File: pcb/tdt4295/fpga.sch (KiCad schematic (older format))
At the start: 1 part

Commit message: start implementing FPGA spi flash
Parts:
- removed U?: XC7A100T-FTG256, symbol FPGA_Xilinx_Artix7:XC7A100T-FTG256
- added J1: FPGA__debug, symbol Connector_Generic:Conn_02x07_Odd_Even
- added U?: XC7A100T-FTG256, symbol FPGA_Xilinx_Artix7:XC7A100T-FTG256
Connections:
- net labels added: GND
- wire segments 0 -> 7
- no-connect marks 23 -> 1
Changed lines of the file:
@@
 $Descr A4 11693 8268
 encoding utf-8
-Sheet 5 5
+Sheet 1 1
 Title ""
 Date ""
@@
 Comment4 ""
 $EndDescr
+NoConn ~ -700 1050
 $Comp
 L FPGA_Xilinx_Artix7:XC7A100T-FTG256 U?
-U 1 1 6142E77A
-P 4650 3800
-F 0 "U?" H 4650 825 50  0000 C CNN
-F 1 "XC7A100T-FTG256" H 4650 734 50  0000 C CNN
-F 2 "" H 4650 3800 50  0001 C CNN
-F 3 "" H 4650 3800 50  0000 C CNN
-	1    4650 3800
+U 3 1 6143113A
+P 4700 3350
+F 0 "U?" H 3420 3403 50  0000 R CNN
+F 1 "XC7A100T-FTG256" H 3420 3312 50  0000 R CNN
+F 2 "" H 4700 3350 50  0001 C CNN
+F 3 "" H 4700 3350 50  0000 C CNN
+	3    4700 3350
+	-1   0    0    -1
+$EndComp
+$Comp
+L Connector_Generic:Conn_02x07_Odd_Even J1
+U 1 1 6145021F
+P 800 2850
+F 0 "J1" H 850 3367 50  0000 C CNN
+F 1 "FPGA__debug" H 850 3276 50  0000 C CNN
+F 2 "" H 800 2850 50  0001 C CNN
+F 3 "~" H 800 2850 50  0001 C CNN
+	1    800  2850
 	1    0    0    -1
 $EndComp
-NoConn ~ 2650 1700
-NoConn ~ 2650 2300
-NoConn ~ 2650 2400
-NoConn ~ 2650 2500
-NoConn ~ 2650 2600
-NoConn ~ 2650 2700
-NoConn ~ 2650 2900
-NoConn ~ 2650 3000
-NoConn ~ 2650 3100
-NoConn ~ 2650 3200
-NoConn ~ 2650 3300
-NoConn ~ 2650 3400
-NoConn ~ 2650 3500
-NoConn ~ 2650 3600
-NoConn ~ 2650 3700
-NoConn ~ 2650 3800
-NoConn ~ 2650 3900
-NoConn ~ 2650 4000
-NoConn ~ 2650 4100
-NoConn ~ 2650 4300
-NoConn ~ 2650 4400
-NoConn ~ 2650 4500
-NoConn ~ -700 1050
+Wire Wire Line
+	600  2550 600  2650
+Connection ~ 600  2650
+Wire Wire Line
+	600  2650 600  2750
+Connection ~ 600  2750
+Wire Wire Line
+	600  2750 600  2850
+Connection ~ 600  2850
+Wire Wire Line
+	600  2850 600  2950
+Connection ~ 600  2950
+Wire Wire Line
+	600  2950 600  3050
+Connection ~ 600  3050
+Wire Wire Line
+	600  3050 600  3150
+Connection ~ 600  3150
+Wire Wire Line
+	600  3150 600  3350
+$Comp
+L power:GND #PWR?
+U 1 1 61452A07
+P 600 3350
+F 0 "#PWR?" H 600 3100 50  0001 C CNN
+F 1 "GND" H 605 3177 50  0000 C CNN
+F 2 "" H 600 3350 50  0001 C CNN
+F 3 "" H 600 3350 50  0001 C CNN
+	1    600  3350
+	1    0    0    -1
+$EndComp
 $EndSCHEMATC

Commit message: fpga and vga
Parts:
- removed U?: XC7A100T-FTG256, symbol FPGA_Xilinx_Artix7:XC7A100T-FTG256
- added C1: 100n, symbol Device:C
- added R1: 2.4k, symbol Device:R
- added R2, R3: 10k, symbol Device:R
- added R4, R5, R6, R8: 4.7k, symbol Device:R
- added R7: 330, symbol Device:R
- added U? (x2): XC7A100T-FTG256-tdt4295, symbol xc7a100t-ftg256-modified:XC7A100T-FTG256-tdt4295
- added U?: S25FL127SABMFV101, SOC008_SPA, symbol S25FL127SABMFV001:S25FL127SABMFV101
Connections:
- net labels added: +1V0, +1V8, +3V3, done, program_b
- wire segments 7 -> 161
- no-connect marks 1 -> 2
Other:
- note added: "TODO: put capacitors for these"
- moved on the sheet: J1

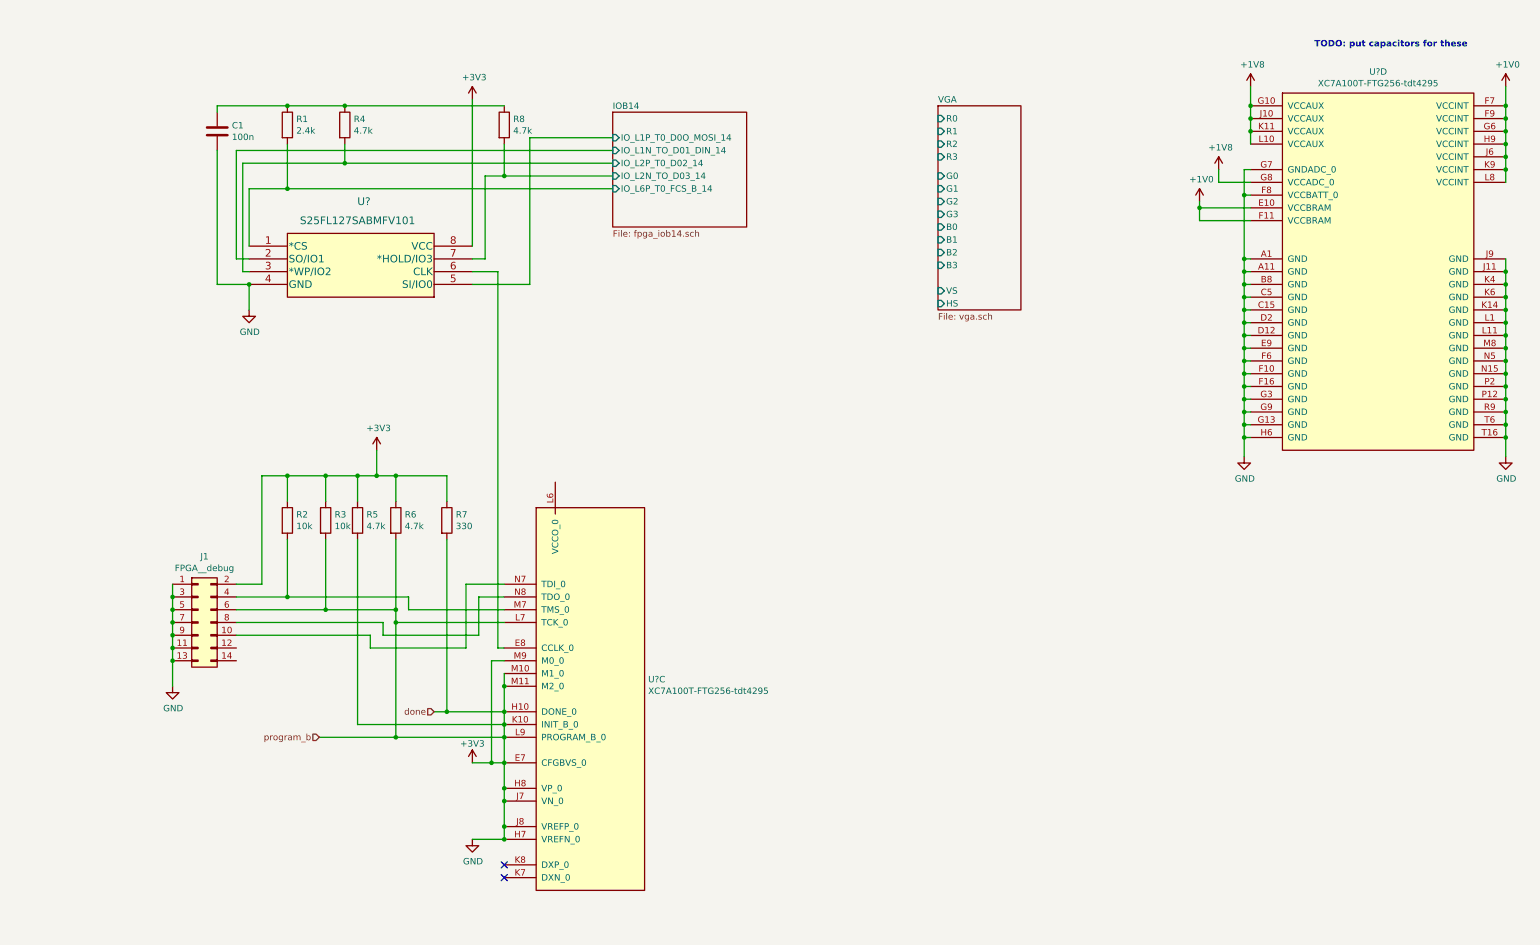
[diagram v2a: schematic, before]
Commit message: fpga external pin headers
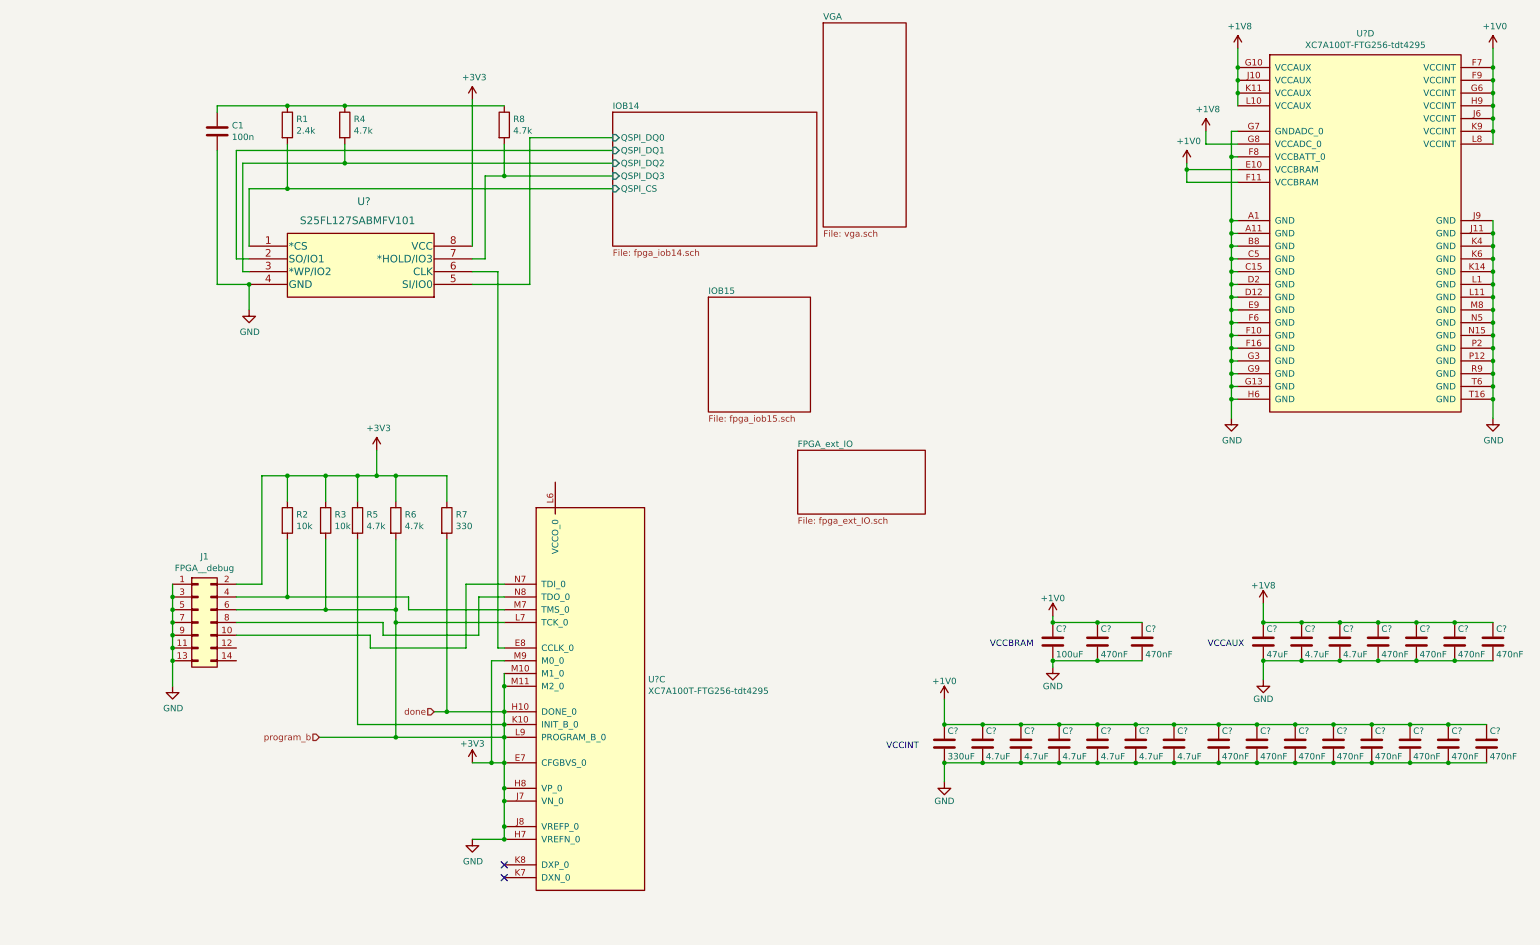
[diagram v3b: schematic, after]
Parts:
- added C?: 100uF, symbol Device:C
- added C?: 47uF, symbol Device:C
- added C? (x8): 4.7uF, symbol Device:C
- added C? (x14): 470nF, symbol Device:C
- added C?: 330uF, symbol Device:C
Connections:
- net +1V0: now also C?.1, C?.1, C?.1, C?.1, C?.1, C?.1, C?.1, C?.1, C?.1, C?.1, C?.1, C?.1, C?.1, C?.1, C?.1, C?.1, C?.1, C?.1
- net +1V8: now also C?.1, C?.1, C?.1, C?.1, C?.1, C?.1, C?.1
- net +3V3: now also C?.2, C?.2, C?.2, C?.2, C?.2, C?.2, C?.2, C?.2, C?.2, C?.2, C?.2, C?.2, C?.2, C?.2, C?.2, C?.2, C?.2, C?.2, C?.2, C?.2, C?.2, C?.2, C?.2, C?.2, C?.2
- net IOB14/IO_L1N_TO_D01_DIN_14 renamed IOB14/QSPI_DQ1
- net IOB14/IO_L1P_T0_D0O_MOSI_14 renamed IOB14/QSPI_DQ0
- net IOB14/IO_L2N_TO_D03_14 renamed IOB14/QSPI_DQ3
- net IOB14/IO_L2P_T0_D02_14 renamed IOB14/QSPI_DQ2
- net IOB14/IO_L6P_T0_FCS_B_14 renamed IOB14/QSPI_CS
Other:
- note added: "VCCAUX"
- note added: "VCCBRAM"
- note added: "VCCINT"
- note removed: "TODO: put capacitors for these"
- moved on the sheet: U?D

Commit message: add another capacitor :)
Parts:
- added C?: 47uF, symbol Device:C
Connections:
- net +3V3: now also C?.1
- net at U?.L6 (VCCO_0): now also C?.2
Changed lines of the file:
@@
 Text Notes 7300 5500 2    50   ~ 0
 VCCBRAM
+$Comp
+L Device:C C?
+U 1 1 61816B10
+P 3550 4050
+F 0 "C?" H 3575 4150 50  0000 L CNN
+F 1 "47uF" H 3575 3950 50  0000 L CNN
+F 2 "" H 3588 3900 50  0001 C CNN
+F 3 "~" H 3550 4050 50  0001 C CNN
+	1    3550 4050
+	1    0    0    -1
+$EndComp
+$Comp
+L power:+3V3 #PWR?
+U 1 1 61822952
+P 3550 3900
+F 0 "#PWR?" H 3550 3750 50  0001 C CNN
+F 1 "+3V3" H 3550 4040 50  0000 C CNN
+F 2 "" H 3550 3900 50  0001 C CNN
+F 3 "" H 3550 3900 50  0001 C CNN
+	1    3550 3900
+	1    0    0    -1
+$EndComp
 $EndSCHEMATC

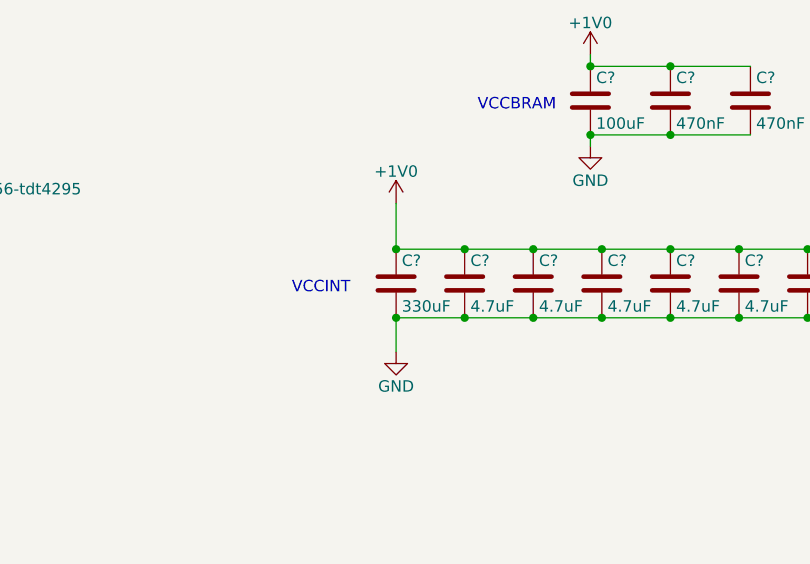
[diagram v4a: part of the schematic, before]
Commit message: Add digikey footprints, implement (some) capacitor footprints in schematic
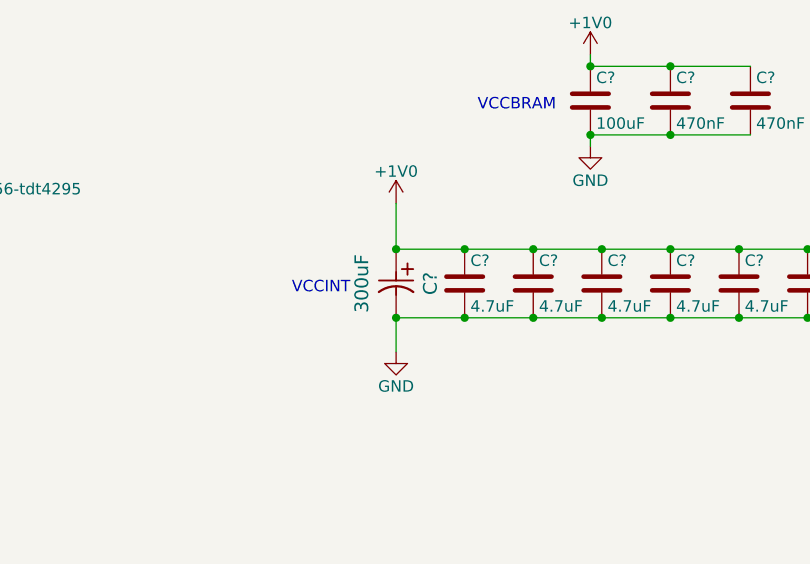
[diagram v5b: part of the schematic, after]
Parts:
- removed C?: 330uF, symbol Device:C
- added C?: 300uF, CAPMP7.6X4.3_1.9N_KEM, symbol T520V337M2R5ATE025:T520V337M2R5ATE025
- C? (x2): footprint (none) -> Capacitor_SMD:C_1210_3225Metric_Pad1.33x2.70mm_HandSolder
- C? (x8): footprint (none) -> Capacitor_SMD:C_0805_2012Metric_Pad1.18x1.45mm_HandSolder
- J1: footprint (none) -> Connector_PinHeader_1.00mm:PinHeader_2x07_P1.00mm_Vertical
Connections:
- net +1V0: now also C?.1
- net +3V3: now also C?.2
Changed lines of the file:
@@
 F 0 "J1" H 800 5817 50  0000 C CNN
 F 1 "FPGA__debug" H 800 5726 50  0000 C CNN
-F 2 "" H 750 5300 50  0001 C CNN
+F 2 "Connector_PinHeader_1.00mm:PinHeader_2x07_P1.00mm_Vertical" H 750 5300 50  0001 C CNN
 F 3 "~" H 750 5300 50  0001 C CNN
 	1    750  5300
@@
 F 0 "C?" H 9425 5550 50  0000 L CNN
 F 1 "4.7uF" H 9425 5350 50  0000 L CNN
-F 2 "" H 9438 5300 50  0001 C CNN
+F 2 "Capacitor_SMD:C_0805_2012Metric_Pad1.18x1.45mm_HandSolder" H 9438 5300 50  0001 C CNN
 F 3 "~" H 9400 5450 50  0001 C CNN
 	1    9400 5450
@@
 F 0 "C?" H 9125 5550 50  0000 L CNN
 F 1 "47uF" H 9125 5350 50  0000 L CNN
-F 2 "" H 9138 5300 50  0001 C CNN
-F 3 "~" H 9100 5450 50  0001 C CNN
+F 2 "Capacitor_SMD:C_1210_3225Metric_Pad1.33x2.70mm_HandSolder" H 9138 5300 50  0001 C CNN
+F 3 "https://search.murata.co.jp/Ceramy/image/img/A01X/G101/ENG/GRM32ER70J476ME20-01.pdf" H 9100 5450 50  0001 C CNN
 	1    9100 5450
 	1    0    0    -1
@@
 F 0 "C?" H 9725 5550 50  0000 L CNN
 F 1 "4.7uF" H 9725 5350 50  0000 L CNN
-F 2 "" H 9738 5300 50  0001 C CNN
+F 2 "Capacitor_SMD:C_0805_2012Metric_Pad1.18x1.45mm_HandSolder" H 9738 5300 50  0001 C CNN
 F 3 "~" H 9700 5450 50  0001 C CNN
 	1    9700 5450
@@
 $Comp
 L Device:C C?
-U 1 1 616BD976
-P 6600 6250
-F 0 "C?" H 6625 6350 50  0000 L CNN
-F 1 "330uF" H 6625 6150 50  0000 L CNN
-F 2 "" H 6638 6100 50  0001 C CNN
-F 3 "~" H 6600 6250 50  0001 C CNN
-	1    6600 6250
-	1    0    0    -1
-$EndComp
-$Comp
-L Device:C C?
 U 1 1 616BDDC2
 P 6900 6250
 F 0 "C?" H 6925 6350 50  0000 L CNN
 F 1 "4.7uF" H 6925 6150 50  0000 L CNN
-F 2 "" H 6938 6100 50  0001 C CNN
-F 3 "~" H 6900 6250 50  0001 C CNN
+F 2 "Capacitor_SMD:C_0805_2012Metric_Pad1.18x1.45mm_HandSolder" H 6938 6100 50  0001 C CNN
+F 3 "C2012X7R1A475K125AC" H 6900 6250 50  0001 C CNN
 	1    6900 6250
 	1    0    0    -1
@@
 F 0 "C?" H 7225 6350 50  0000 L CNN
 F 1 "4.7uF" H 7225 6150 50  0000 L CNN
-F 2 "" H 7238 6100 50  0001 C CNN
-F 3 "~" H 7200 6250 50  0001 C CNN
+F 2 "Capacitor_SMD:C_0805_2012Metric_Pad1.18x1.45mm_HandSolder" H 7238 6100 50  0001 C CNN
+F 3 "" H 7200 6250 50  0001 C CNN
 	1    7200 6250
 	1    0    0    -1
@@
 F 0 "C?" H 7525 6350 50  0000 L CNN
 F 1 "4.7uF" H 7525 6150 50  0000 L CNN
-F 2 "" H 7538 6100 50  0001 C CNN
+F 2 "Capacitor_SMD:C_0805_2012Metric_Pad1.18x1.45mm_HandSolder" H 7538 6100 50  0001 C CNN
 F 3 "~" H 7500 6250 50  0001 C CNN
 	1    7500 6250
@@
 F 0 "C?" H 7825 6350 50  0000 L CNN
 F 1 "4.7uF" H 7825 6150 50  0000 L CNN
-F 2 "" H 7838 6100 50  0001 C CNN
+F 2 "Capacitor_SMD:C_0805_2012Metric_Pad1.18x1.45mm_HandSolder" H 7838 6100 50  0001 C CNN
 F 3 "~" H 7800 6250 50  0001 C CNN
 	1    7800 6250
@@
 F 0 "C?" H 8125 6350 50  0000 L CNN
 F 1 "4.7uF" H 8125 6150 50  0000 L CNN
-F 2 "" H 8138 6100 50  0001 C CNN
+F 2 "Capacitor_SMD:C_0805_2012Metric_Pad1.18x1.45mm_HandSolder" H 8138 6100 50  0001 C CNN
 F 3 "~" H 8100 6250 50  0001 C CNN
 	1    8100 6250
@@
 F 0 "C?" H 8425 6350 50  0000 L CNN
 F 1 "4.7uF" H 8425 6150 50  0000 L CNN
-F 2 "" H 8438 6100 50  0001 C CNN
+F 2 "Capacitor_SMD:C_0805_2012Metric_Pad1.18x1.45mm_HandSolder" H 8438 6100 50  0001 C CNN
 F 3 "~" H 8400 6250 50  0001 C CNN
 	1    8400 6250
@@
 F 0 "C?" H 7475 5550 50  0000 L CNN
 F 1 "100uF" H 7475 5350 50  0000 L CNN
-F 2 "" H 7488 5300 50  0001 C CNN
-F 3 "~" H 7450 5450 50  0001 C CNN
+F 2 "Capacitor_SMD:C_1210_3225Metric_Pad1.33x2.70mm_HandSolder" H 7488 5300 50  0001 C CNN
+F 3 "https://api.kemet.com/component-edge/download/specsheet/C1210C107M9PACTU.pdf" H 7450 5450 50  0001 C CNN
 	1    7450 5450
 	1    0    0    -1
@@
 	1    0    0    -1
 $EndComp
+$Comp
+L T520V337M2R5ATE025:T520V337M2R5ATE025 C?
+U 1 1 614CD791
+P 6600 6100
+F 0 "C?" H 6750 6250 60  0000 C CNN
+F 1 "300uF" H 6750 5950 60  0000 C CNN
+F 2 "CAPMP7.6X4.3_1.9N_KEM" H 6750 5740 60  0001 C CNN
+F 3 "" H 6600 6100 60  0000 C CNN
+F 4 "T520V337M2R5ATE025" H 6600 6100 50  0001 C CNN "Component name"
+	1    6600 6100
+	0    1    1    0
+$EndComp
 $EndSCHEMATC
